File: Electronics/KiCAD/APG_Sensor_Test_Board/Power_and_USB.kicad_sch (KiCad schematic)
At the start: 0 parts

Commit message: Gannon inspection decision to change IMU
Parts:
- added C13: 1µF, symbol Device:C_Small
- added C14, C15, C16, C17: 1u, symbol Device:C_Small
- added FB1: 330Ω, symbol Device:FerriteBead
- added J1: USB_C_Receptacle_USB2.0_16P, symbol Connector:USB_C_Receptacle_USB2.0_16P
- added R10, R9: 5.1k, symbol Device:R_US
- added U4: MCP1700x-180xxTT, Package_TO_SOT_SMD:SOT-23, symbol Regulator_Linear:MCP1700x-180xxTT
- added U5: TLV1117-33, symbol Regulator_Linear:TLV1117-33
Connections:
- new net: J1.A5 (CC1), R10.1
- new net: FB1.1, J1.A4 (VBUS), J1.A9 (VBUS), J1.B4 (VBUS), J1.B9 (VBUS)
- new net: J1.B5 (CC2), R9.1
- new net +1V8: C17.1, U4.2 (VO)
- new net +3V3: C15.1, U5.2 (VO)
- new net +5V: C13.1, C14.1, C16.1, FB1.2, U4.3 (VI), U5.3 (VI)
- new net D_N: J1.A7 (D-), J1.B7 (D-)
- new net D_P: J1.A6 (D+), J1.B6 (D+)
- new net GND: C13.2, C14.2, C15.2, C16.2, C17.2, J1.A1 (GND), J1.A12 (GND), J1.B1 (GND), J1.B12 (GND), J1.S1 (SHIELD), R10.2, R9.2, U5.1 (GND)
- no-connect marks 0 -> 2

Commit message: Main Schematic Complete
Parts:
- removed C16, C17: 1u, symbol Device:C_Small
- removed U4: MCP1700x-180xxTT, Package_TO_SOT_SMD:SOT-23, symbol Regulator_Linear:MCP1700x-180xxTT

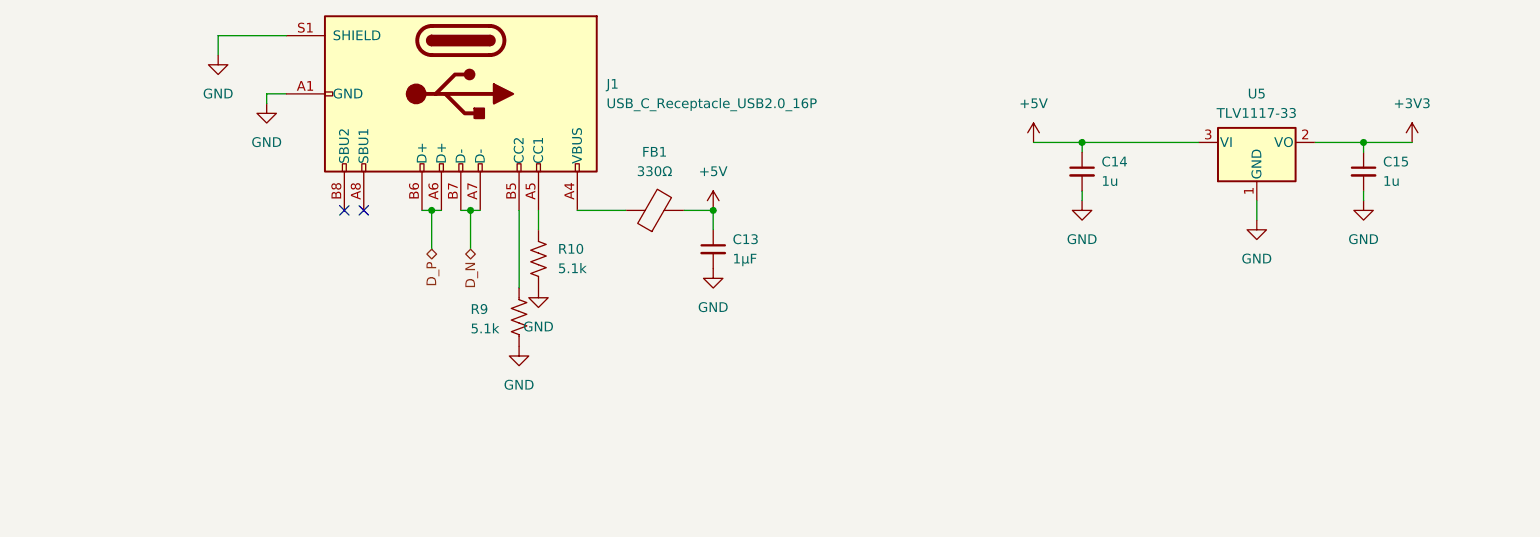
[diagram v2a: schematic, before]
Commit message: reaninotate and begin footprints
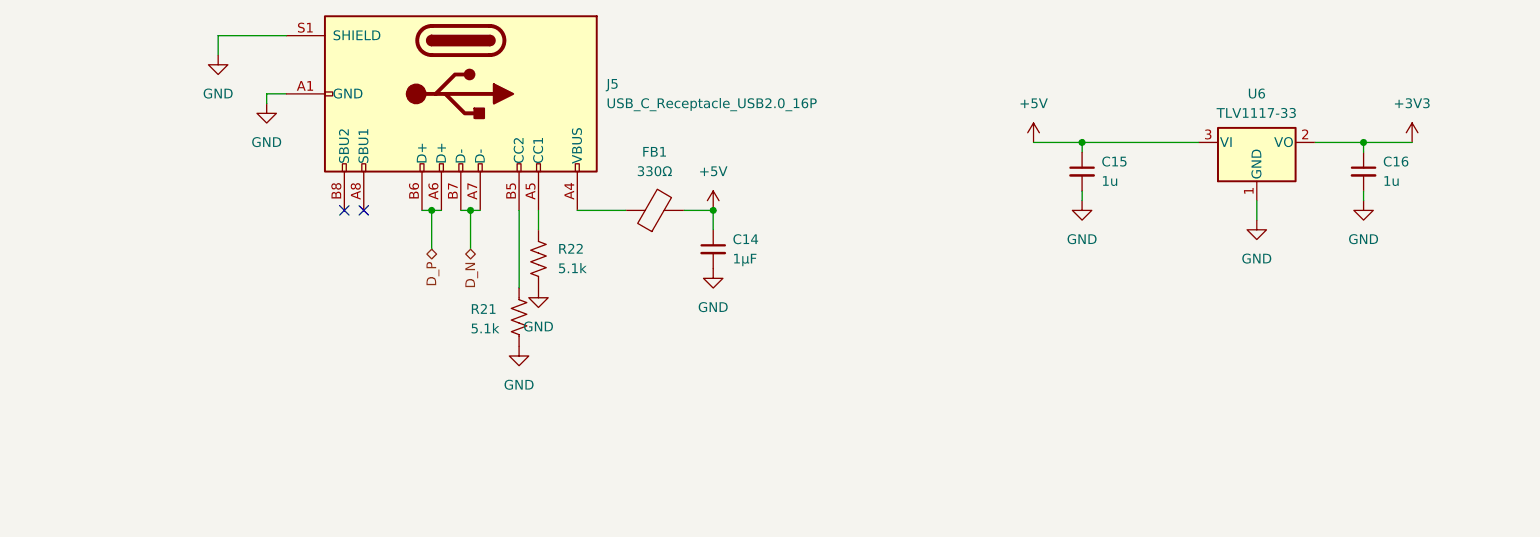
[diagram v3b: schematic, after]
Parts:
- C14: renamed from C13; footprint (none) -> Capacitor_SMD:C_0805_2012Metric
- C15: renamed from C14; footprint (none) -> Capacitor_SMD:C_0805_2012Metric
- C16: renamed from C15; footprint (none) -> Capacitor_SMD:C_0805_2012Metric
- FB1: footprint (none) -> Resistor_SMD:R_0805_2012Metric
- J5: renamed from J1; footprint (none) -> Connector_USB:USB_C_Receptacle_GCT_USB4105-xx-A_16P_TopMnt_Horizontal; DigiKey Part # (none) -> USB4105-GF-A
- R21: renamed from R9; footprint (none) -> Resistor_SMD:R_0805_2012Metric
- R22: renamed from R10; footprint (none) -> Resistor_SMD:R_0805_2012Metric
- renumbered U5 to U6
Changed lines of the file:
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@@
 		(dnp no)
 		(fields_autoplaced yes)
-		(property "Reference" "#PWR034"
+		(property "Reference" "#PWR045"
 			(at 63.5 68.58 0)
 			(effects
@@
 			(project "APG_Sensor_Test_Board"
 				(path "/3161be0c-372f-463d-be0a-bab00f344057/ce24b18a-13e5-44eb-9a8e-7d29741d4106"
-					(reference "#PWR034")
+					(reference "#PWR045")
 					(unit 1)
 				)
@@
 		(dnp no)
 		(fields_autoplaced yes)
-		(property "Reference" "#PWR043"
+		(property "Reference" "#PWR054"
 			(at 213.36 87.63 0)
 			(effects
@@
 			(project "APG_Sensor_Test_Board"
 				(path "/3161be0c-372f-463d-be0a-bab00f344057/ce24b18a-13e5-44eb-9a8e-7d29741d4106"
-					(reference "#PWR043")
+					(reference "#PWR054")
 					(unit 1)
 				)
@@
 		(dnp no)
 		(fields_autoplaced yes)
-		(property "Reference" "R10"
+		(property "Reference" "R22"
 			(at 107.95 87.6299 0)
 			(effects
@@
 			)
 		)
-		(property "Footprint" ""
+		(property "Footprint" "Resistor_SMD:R_0805_2012Metric"
 			(at 106.426 89.154 90)
 			(effects
@@
 			(project "APG_Sensor_Test_Board"
 				(path "/3161be0c-372f-463d-be0a-bab00f344057/ce24b18a-13e5-44eb-9a8e-7d29741d4106"
-					(reference "R10")
+					(reference "R22")
 					(unit 1)
 				)
@@
 		(dnp no)
 		(fields_autoplaced yes)
-		(property "Reference" "C15"
+		(property "Reference" "C16"
 			(at 215.9 76.2062 0)
 			(effects
@@
 			)
 		)
-		(property "Footprint" ""
+		(property "Footprint" "Capacitor_SMD:C_0805_2012Metric"
 			(at 213.36 77.47 0)
 			(effects
@@
 			(project "APG_Sensor_Test_Board"
 				(path "/3161be0c-372f-463d-be0a-bab00f344057/ce24b18a-13e5-44eb-9a8e-7d29741d4106"
-					(reference "C15")
+					(reference "C16")
 					(unit 1)
 				)
@@
 		(on_board yes)
 		(dnp no)
-		(property "Reference" "#PWR037"
+		(property "Reference" "#PWR048"
 			(at 105.41 99.06 0)
 			(effects
@@
 			(project "APG_Sensor_Test_Board"
 				(path "/3161be0c-372f-463d-be0a-bab00f344057/ce24b18a-13e5-44eb-9a8e-7d29741d4106"
-					(reference "#PWR037")
+					(reference "#PWR048")
 					(unit 1)
 				)
@@
 		(dnp no)
 		(fields_autoplaced yes)
-		(property "Reference" "C13"
+		(property "Reference" "C14"
 			(at 130.81 86.3662 0)
 			(effects
@@
 			)
 		)
-		(property "Footprint" ""
+		(property "Footprint" "Capacitor_SMD:C_0805_2012Metric"
 			(at 128.27 87.63 0)
 			(effects
@@
 			(project "APG_Sensor_Test_Board"
 				(path "/3161be0c-372f-463d-be0a-bab00f344057/ce24b18a-13e5-44eb-9a8e-7d29741d4106"
-					(reference "C13")
+					(reference "C14")
 					(unit 1)
 				)
@@
 		(dnp no)
 		(fields_autoplaced yes)
-		(property "Reference" "C14"
+		(property "Reference" "C15"
 			(at 179.07 76.2062 0)
 			(effects
@@
 			)
 		)
-		(property "Footprint" ""
+		(property "Footprint" "Capacitor_SMD:C_0805_2012Metric"
 			(at 176.53 77.47 0)
 			(effects
@@
 			(project "APG_Sensor_Test_Board"
 				(path "/3161be0c-372f-463d-be0a-bab00f344057/ce24b18a-13e5-44eb-9a8e-7d29741d4106"
-					(reference "C14")
+					(reference "C15")
 					(unit 1)
 				)
@@
 			)
 		)
-		(property "Footprint" ""
+		(property "Footprint" "Resistor_SMD:R_0805_2012Metric"
 			(at 120.65 84.328 90)
 			(effects
@@
 		(dnp no)
 		(fields_autoplaced yes)
-		(property "Reference" "#PWR035"
+		(property "Reference" "#PWR046"
 			(at 69.85 74.93 0)
 			(effects
@@
 			(project "APG_Sensor_Test_Board"
 				(path "/3161be0c-372f-463d-be0a-bab00f344057/ce24b18a-13e5-44eb-9a8e-7d29741d4106"
-					(reference "#PWR035")
+					(reference "#PWR046")
 					(unit 1)
 				)
@@
 		(on_board yes)
 		(dnp no)
-		(property "Reference" "#PWR039"
+		(property "Reference" "#PWR050"
 			(at 128.27 96.52 0)
 			(effects
@@
 			(project "APG_Sensor_Test_Board"
 				(path "/3161be0c-372f-463d-be0a-bab00f344057/ce24b18a-13e5-44eb-9a8e-7d29741d4106"
-					(reference "#PWR039")
+					(reference "#PWR050")
 					(unit 1)
 				)
@@
 		(dnp no)
 		(fields_autoplaced yes)
-		(property "Reference" "U5"
+		(property "Reference" "U6"
 			(at 199.39 67.31 0)
 			(effects
@@
 			(project ""
 				(path "/3161be0c-372f-463d-be0a-bab00f344057/ce24b18a-13e5-44eb-9a8e-7d29741d4106"
-					(reference "U5")
+					(reference "U6")
 					(unit 1)
 				)
@@
 		(on_board yes)
 		(dnp no)
-		(property "Reference" "R9"
+		(property "Reference" "R21"
 			(at 96.52 95.504 0)
 			(effects
@@
 			)
 		)
-		(property "Footprint" ""
+		(property "Footprint" "Resistor_SMD:R_0805_2012Metric"
 			(at 103.886 96.774 90)
 			(effects
@@
 			(project "APG_Sensor_Test_Board"
 				(path "/3161be0c-372f-463d-be0a-bab00f344057/ce24b18a-13e5-44eb-9a8e-7d29741d4106"
-					(reference "R9")
+					(reference "R21")
 					(unit 1)
 				)
@@
 		(dnp no)
 		(fields_autoplaced yes)
-		(property "Reference" "#PWR041"
+		(property "Reference" "#PWR052"
 			(at 176.53 87.63 0)
 			(effects
@@
 			(project "APG_Sensor_Test_Board"
 				(path "/3161be0c-372f-463d-be0a-bab00f344057/ce24b18a-13e5-44eb-9a8e-7d29741d4106"
-					(reference "#PWR041")
+					(reference "#PWR052")
 					(unit 1)
 				)
@@
 		(dnp no)
 		(fields_autoplaced yes)
-		(property "Reference" "#PWR036"
+		(property "Reference" "#PWR047"
 			(at 102.87 106.68 0)
 			(effects
@@
 			(project "APG_Sensor_Test_Board"
 				(path "/3161be0c-372f-463d-be0a-bab00f344057/ce24b18a-13e5-44eb-9a8e-7d29741d4106"
-					(reference "#PWR036")
+					(reference "#PWR047")
 					(unit 1)
 				)
@@
 		(dnp no)
 		(fields_autoplaced yes)
-		(property "Reference" "#PWR042"
+		(property "Reference" "#PWR053"
 			(at 199.39 90.17 0)
 			(effects
@@
 			(project "APG_Sensor_Test_Board"
 				(path "/3161be0c-372f-463d-be0a-bab00f344057/ce24b18a-13e5-44eb-9a8e-7d29741d4106"
-					(reference "#PWR042")
+					(reference "#PWR053")
 					(unit 1)
 				)
@@
 		(dnp no)
 		(fields_autoplaced yes)
-		(property "Reference" "#PWR038"
+		(property "Reference" "#PWR049"
 			(at 128.27 86.36 0)
 			(effects
@@
 			(project "APG_Sensor_Test_Board"
 				(path "/3161be0c-372f-463d-be0a-bab00f344057/ce24b18a-13e5-44eb-9a8e-7d29741d4106"
-					(reference "#PWR038")
+					(reference "#PWR049")
 					(unit 1)
 				)
@@
 		(dnp no)
 		(fields_autoplaced yes)
-		(property "Reference" "J1"
+		(property "Reference" "J5"
 			(at 114.3 66.0399 90)
 			(effects
@@
 			)
 		)
-		(property "Footprint" ""
+		(property "Footprint" "Connector_USB:USB_C_Receptacle_GCT_USB4105-xx-A_16P_TopMnt_Horizontal"
 			(at 95.25 71.12 0)
 			(effects
@@
 			)
 		)
+		(property "DigiKey Part #" "USB4105-GF-A"
+			(at 95.25 67.31 90)
+			(effects
+				(font
+					(size 1.27 1.27)
+				)
+				(hide yes)
+			)
+		)
 		(pin "S1"
 		)
@@
 			(project "APG_Sensor_Test_Board"
 				(path "/3161be0c-372f-463d-be0a-bab00f344057/ce24b18a-13e5-44eb-9a8e-7d29741d4106"
-					(reference "J1")
+					(reference "J5")
 					(unit 1)
 				)
@@
 		(dnp no)
 		(fields_autoplaced yes)
-		(property "Reference" "#PWR044"
+		(property "Reference" "#PWR055"
 			(at 219.71 77.47 0)
 			(effects
@@
 			(project ""
 				(path "/3161be0c-372f-463d-be0a-bab00f344057/ce24b18a-13e5-44eb-9a8e-7d29741d4106"
-					(reference "#PWR044")
+					(reference "#PWR055")
 					(unit 1)
 				)
@@
 		(dnp no)
 		(fields_autoplaced yes)
-		(property "Reference" "#PWR040"
+		(property "Reference" "#PWR051"
 			(at 170.18 77.47 0)
 			(effects
@@
 			(project "APG_Sensor_Test_Board"
 				(path "/3161be0c-372f-463d-be0a-bab00f344057/ce24b18a-13e5-44eb-9a8e-7d29741d4106"
-					(reference "#PWR040")
-					(unit 1)
-				)
+					(reference "#PWR051")
+					(unit 1)
+				)

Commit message: completed footprint assignment
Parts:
- U6: footprint (none) -> Package_TO_SOT_SMD:SOT-223-3_TabPin2
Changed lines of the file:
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@@
 			)
 		)
-		(property "Footprint" ""
+		(property "Footprint" "Package_TO_SOT_SMD:SOT-223-3_TabPin2"
 			(at 199.39 73.66 0)
 			(effects

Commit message: JLC part numbers
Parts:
- U6: JLCPCB (none) -> C37359
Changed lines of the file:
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@@
+			)
+		)
+		(property "JLCPCB" "C37359"
+			(at 199.39 73.66 0)
+			(effects
+				(font
+					(size 1.27 1.27)
+				)
+				(hide yes)
 			)
 		)

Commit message: added test points
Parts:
- added TP6: +3.3V, symbol Connector:TestPoint
- added TP7: 5V, symbol Connector:TestPoint
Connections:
- net +3V3: now also TP6.1
- net +5V: now also TP7.1
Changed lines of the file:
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@@
 	(paper "A4")
+	(junction
+		(at 224.79 73.66)
+		(diameter 0)
+		(color 0 0 0 0)
+	)
 	(junction
 		(at 128.27 82.55)
@@
 	(wire
 		(pts
+			(xy 224.79 73.66) (xy 224.79 77.47)
+		)
+		(stroke
+			(width 0)
+			(type default)
+		)
+	)
+	(wire
+		(pts
 			(xy 96.52 82.55) (xy 97.79 82.55)
 		)
@@
 	(wire
 		(pts
+			(xy 128.27 82.55) (xy 138.43 82.55)
+		)
+		(stroke
+			(width 0)
+			(type default)
+		)
+	)
+	(wire
+		(pts
 			(xy 72.39 59.69) (xy 63.5 59.69)
 		)
@@
 	(wire
 		(pts
-			(xy 213.36 73.66) (xy 219.71 73.66)
+			(xy 213.36 73.66) (xy 224.79 73.66)
 		)
 		(stroke
@@
 	)
 	(symbol
+		(lib_id "Connector:TestPoint")
+		(at 138.43 82.55 180)
+		(unit 1)
+		(exclude_from_sim no)
+		(in_bom yes)
+		(on_board yes)
+		(dnp no)
+		(fields_autoplaced yes)
+		(property "Reference" "TP7"
+			(at 140.97 84.5819 0)
+			(effects
+				(font
+					(size 1.27 1.27)
+				)
+				(justify right)
+			)
+		)
+		(property "Value" "5V"
+			(at 140.97 87.1219 0)
+			(effects
+				(font
+					(size 1.27 1.27)
+				)
+				(justify right)
+			)
+		)
+		(property "Footprint" ""
+			(at 133.35 82.55 0)
+			(effects
+				(font
+					(size 1.27 1.27)
+				)
+				(hide yes)
+			)
+		)
+		(property "Datasheet" "~"
+			(at 133.35 82.55 0)
+			(effects
+				(font
+					(size 1.27 1.27)
+				)
+				(hide yes)
+			)
+		)
+		(property "Description" "test point"
+			(at 138.43 82.55 0)
+			(effects
+				(font
+					(size 1.27 1.27)
+				)
+				(hide yes)
+			)
+		)
+		(pin "1"
+		)
+		(instances
+			(project "APG_Sensor_Test_Board"
+				(path "/3161be0c-372f-463d-be0a-bab00f344057/ce24b18a-13e5-44eb-9a8e-7d29741d4106"
+					(reference "TP7")
+					(unit 1)
+				)
+			)
+		)
+	)
+	(symbol
+		(lib_id "Connector:TestPoint")
+		(at 224.79 77.47 180)
+		(unit 1)
+		(exclude_from_sim no)
+		(in_bom yes)
+		(on_board yes)
+		(dnp no)
+		(fields_autoplaced yes)
+		(property "Reference" "TP6"
+			(at 227.33 79.5019 0)
+			(effects
+				(font
+					(size 1.27 1.27)
+				)
+				(justify right)
+			)
+		)
+		(property "Value" "+3.3V"
+			(at 227.33 82.0419 0)
+			(effects
+				(font
+					(size 1.27 1.27)
+				)
+				(justify right)
+			)
+		)
+		(property "Footprint" ""
+			(at 219.71 77.47 0)
+			(effects
+				(font
+					(size 1.27 1.27)
+				)
+				(hide yes)
+			)
+		)
+		(property "Datasheet" "~"
+			(at 219.71 77.47 0)
+			(effects
+				(font
+					(size 1.27 1.27)
+				)
+				(hide yes)
+			)
+		)
+		(property "Description" "test point"
+			(at 224.79 77.47 0)
+			(effects
+				(font
+					(size 1.27 1.27)
+				)
+				(hide yes)
+			)
+		)
+		(pin "1"
+		)
+		(instances
+			(project "APG_Sensor_Test_Board"
+				(path "/3161be0c-372f-463d-be0a-bab00f344057/ce24b18a-13e5-44eb-9a8e-7d29741d4106"
+					(reference "TP6")
+					(unit 1)
+				)
+			)
+		)
+	)
+	(symbol
 		(lib_id "Device:R_US")
 		(at 105.41 88.9 0)
@@
 	(symbol
 		(lib_id "power:+3V3")
-		(at 219.71 73.66 0)
+		(at 224.79 73.66 0)
 		(unit 1)
 		(exclude_from_sim no)
@@
 		(fields_autoplaced yes)
 		(property "Reference" "#PWR055"
-			(at 219.71 77.47 0)
+			(at 224.79 77.47 0)
 			(effects
 				(font
@@
 		)
 		(property "Value" "+3V3"
-			(at 219.71 68.58 0)
+			(at 224.79 68.58 0)
 			(effects
 				(font
@@
 		)
 		(property "Footprint" ""
-			(at 219.71 73.66 0)
+			(at 224.79 73.66 0)
 			(effects
 				(font
@@
 		)
 		(property "Datasheet" ""
-			(at 219.71 73.66 0)
+			(at 224.79 73.66 0)
 			(effects
 				(font
@@
 		)
 		(property "Description" "Power symbol creates a global label with name \"+3V3\""
-			(at 219.71 73.66 0)
-			(effects
-				(font
+			(at 224.79 73.66 0)
+			(effects
+				(font

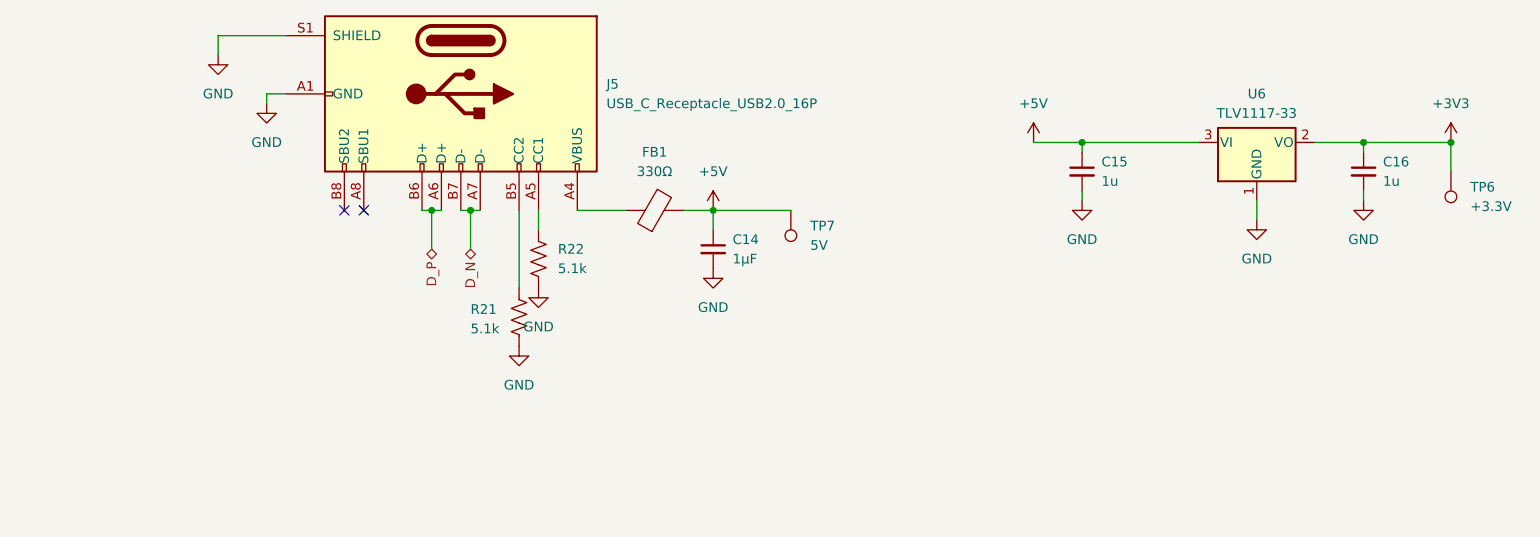
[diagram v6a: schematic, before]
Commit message: MOved IMU and HIGH G to SPI other misc changes
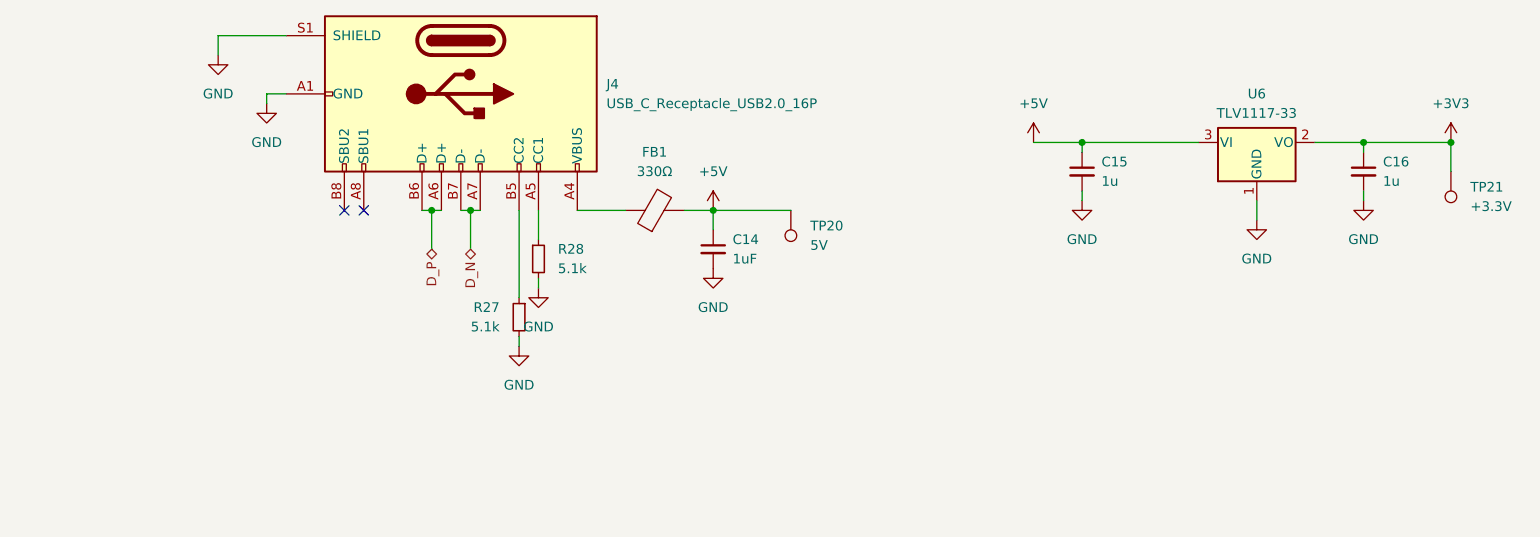
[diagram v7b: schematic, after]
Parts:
- removed R21, R22: 5.1k, Resistor_SMD:R_0805_2012Metric, symbol Device:R_US
- added R27, R28: 5.1k, Resistor_SMD:R_0805_2012Metric, symbol Device:R_Small
- C14: value 1µF -> 1uF
- TP20: renamed from TP7; footprint (none) -> TestPoint:TestPoint_Pad_3.0x3.0mm
- TP21: renamed from TP6; footprint (none) -> TestPoint:TestPoint_Pad_3.0x3.0mm
- renumbered J5 to J4
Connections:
- net GND: now also R27.2, R28.2
- net at J4.A5 (CC1): now also R28.1
- net at J4.B5 (CC2): now also R27.1
